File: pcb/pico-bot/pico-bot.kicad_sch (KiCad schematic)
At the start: 58 parts, among them J1 Conn_01x02_Male, J2 Conn_01x06_Male, J3 Conn_01x06_Male, J4 Conn_01x06_Male, J5 Conn_01x04_Male, Q1 DMG2305UX, Q2 AOD417, SW1 SW_SPDT, SW2 SW_Push, SW3 SW_Push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

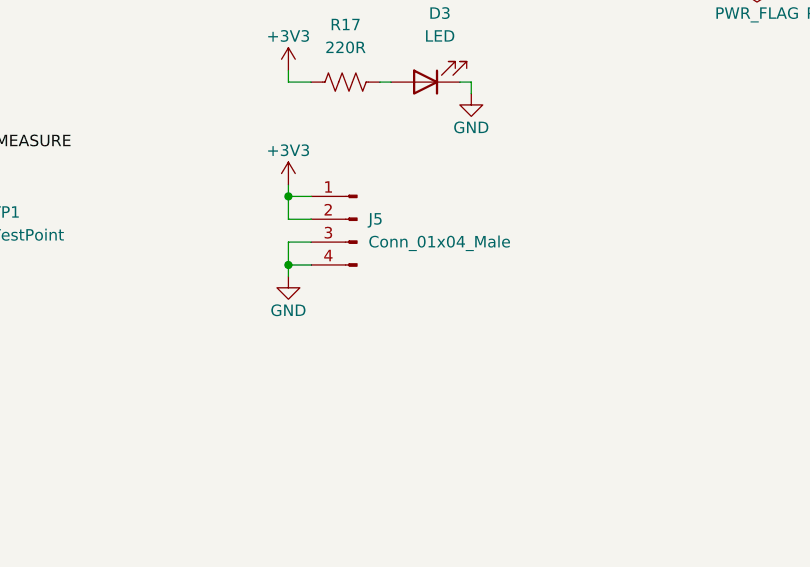
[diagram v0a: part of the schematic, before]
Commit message: Fix missing footprints, add parts to PCB
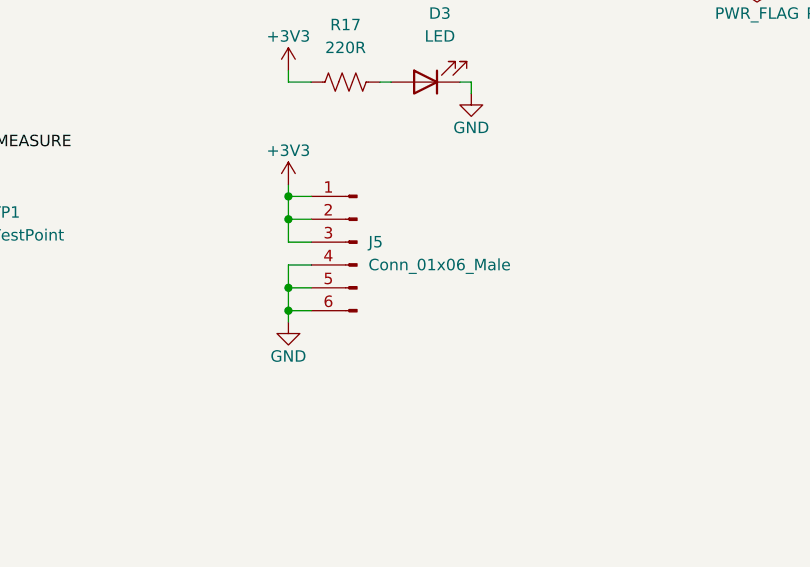
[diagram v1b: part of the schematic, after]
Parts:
- removed J5: Conn_01x04_Male, symbol Connector:Conn_01x04_Male
- added J5: Conn_01x06_Male, Connector_PinHeader_2.54mm:PinHeader_2x03_P2.54mm_Vertical, symbol Connector:Conn_01x06_Male
- J4: footprint Connector_PinHeader_2.54mm:PinHeader_1x06_P2.54mm_Vertical -> Connector_PinHeader_2.54mm:PinHeader_2x03_P2.54mm_Vertical
- SW1: footprint (none) -> pico-bot:1101M2S3CRE2
- U4: footprint RPi_Pico:RPi_Pico_SMD_TH -> pico-bot:RPi_Pico_SMD_TH
- U5: footprint (none) -> Package_SO:SOIC-8-1EP_3.9x4.9mm_P1.27mm_EP2.29x3mm
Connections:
- net +3V3: now also J5.1 (Pin_1), J5.2 (Pin_2), J5.3 (Pin_3)
- net GND: now also J5.4 (Pin_4), J5.5 (Pin_5), J5.6 (Pin_6)
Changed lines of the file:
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@@
   (junction (at 182.88 148.59) (diameter 0) (color 0 0 0 0)
   )
-  (junction (at 281.94 86.36) (diameter 0) (color 0 0 0 0)
+  (junction (at 281.94 91.44) (diameter 0) (color 0 0 0 0)
   )
   (junction (at 308.61 233.68) (diameter 0) (color 0 0 0 0)
@@
   (junction (at 171.45 39.37) (diameter 0) (color 0 0 0 0)
   )
+  (junction (at 281.94 81.28) (diameter 0) (color 0 0 0 0)
+  )
   (junction (at 181.61 39.37) (diameter 0) (color 0 0 0 0)
   )
@@
   (junction (at 171.45 50.8) (diameter 0) (color 0 0 0 0)
   )
+  (junction (at 281.94 88.9) (diameter 0) (color 0 0 0 0)
+  )
   (junction (at 281.94 78.74) (diameter 0) (color 0 0 0 0)
   )
@@
     (stroke (width 0) (type default) (color 0 0 0 0))
   )
-  (wire (pts (xy 281.94 86.36) (xy 281.94 87.63))
+  (wire (pts (xy 281.94 91.44) (xy 281.94 92.71))
     (stroke (width 0) (type default) (color 0 0 0 0))
   )
@@
     (stroke (width 0) (type default) (color 0 0 0 0))
   )
+  (wire (pts (xy 284.48 86.36) (xy 281.94 86.36))
+    (stroke (width 0) (type default) (color 0 0 0 0))
+  )
   (wire (pts (xy 217.17 185.42) (xy 217.17 184.15))
     (stroke (width 0) (type default) (color 0 0 0 0))
@@
     (stroke (width 0) (type default) (color 0 0 0 0))
   )
+  (wire (pts (xy 281.94 86.36) (xy 281.94 88.9))
+    (stroke (width 0) (type default) (color 0 0 0 0))
+  )
   (wire (pts (xy 247.65 205.74) (xy 248.92 205.74))
     (stroke (width 0) (type default) (color 0 0 0 0))
@@
     (stroke (width 0) (type default) (color 0 0 0 0))
   )
-  (wire (pts (xy 281.94 83.82) (xy 281.94 86.36))
+  (wire (pts (xy 281.94 88.9) (xy 281.94 91.44))
     (stroke (width 0) (type default) (color 0 0 0 0))
   )
@@
     (stroke (width 0) (type default) (color 0 0 0 0))
   )
-  (wire (pts (xy 281.94 86.36) (xy 284.48 86.36))
+  (wire (pts (xy 281.94 91.44) (xy 284.48 91.44))
     (stroke (width 0) (type default) (color 0 0 0 0))
   )
@@
     (stroke (width 0) (type default) (color 0 0 0 0))
   )
+  (wire (pts (xy 284.48 83.82) (xy 281.94 83.82))
+    (stroke (width 0) (type default) (color 0 0 0 0))
+  )
   (wire (pts (xy 307.34 228.6) (xy 308.61 228.6))
     (stroke (width 0) (type default) (color 0 0 0 0))
@@
     (stroke (width 0) (type default) (color 0 0 0 0))
   )
+  (wire (pts (xy 281.94 83.82) (xy 281.94 81.28))
+    (stroke (width 0) (type default) (color 0 0 0 0))
+  )
   (wire (pts (xy 259.08 205.74) (xy 260.35 205.74))
     (stroke (width 0) (type default) (color 0 0 0 0))
@@
     (stroke (width 0) (type default) (color 0 0 0 0))
   )
-  (wire (pts (xy 284.48 83.82) (xy 281.94 83.82))
+  (wire (pts (xy 284.48 88.9) (xy 281.94 88.9))
     (stroke (width 0) (type default) (color 0 0 0 0))
   )
@@
     (property "Reference" "SW1" (id 0) (at 148.59 34.29 0))
     (property "Value" "SW_SPDT" (id 1) (at 148.59 36.83 0))
-    (property "Footprint" "" (id 2) (at 148.59 41.91 0)
+    (property "Footprint" "pico-bot:1101M2S3CRE2" (id 2) (at 148.59 41.91 0)
       (effects (font (size 1.27 1.27)) hide)
     )
@@
     (property "Reference" "U5" (id 0) (at 231.14 63.5 0))
     (property "Value" "TL062" (id 1) (at 231.14 66.04 0))
-    (property "Footprint" "" (id 2) (at 231.14 73.66 0)
+    (property "Footprint" "Package_SO:SOIC-8-1EP_3.9x4.9mm_P1.27mm_EP2.29x3mm" (id 2) (at 231.14 73.66 0)
       (effects (font (size 1.27 1.27)) hide)
     )
@@
     (pin "2")
   )
-  (symbol (lib_id "Connector:Conn_01x04_Male") (at 289.56 81.28 0) (mirror y) (unit 1)
-    (in_bom yes) (on_board yes) (fields_autoplaced)
-    (property "Reference" "J5" (id 0) (at 290.83 81.2799 0)
-      (effects (font (size 1.27 1.27)) (justify right))
-    )
-    (property "Value" "Conn_01x04_Male" (id 1) (at 290.83 83.8199 0)
-      (effects (font (size 1.27 1.27)) (justify right))
-    )
-    (property "Footprint" "" (id 2) (at 289.56 81.28 0)
-      (effects (font (size 1.27 1.27)) hide)
-    )
-    (property "Datasheet" "~" (id 3) (at 289.56 81.28 0)
-      (effects (font (size 1.27 1.27)) hide)
-    )
-    (pin "1")
-    (pin "2")
-    (pin "3")
-    (pin "4")
-  )
   (symbol (lib_id "Device:C") (at 297.18 185.42 180) (unit 1)
     (in_bom yes) (on_board yes) (fields_autoplaced)
@@
     (pin "2")
   )
+  (symbol (lib_id "Connector:Conn_01x06_Male") (at 289.56 83.82 0) (mirror y) (unit 1)
+    (in_bom yes) (on_board yes) (fields_autoplaced)
+    (property "Reference" "J5" (id 0) (at 290.83 83.8199 0)
+      (effects (font (size 1.27 1.27)) (justify right))
+    )
+    (property "Value" "Conn_01x06_Male" (id 1) (at 290.83 86.3599 0)
+      (effects (font (size 1.27 1.27)) (justify right))
+    )
+    (property "Footprint" "Connector_PinHeader_2.54mm:PinHeader_2x03_P2.54mm_Vertical" (id 2) (at 289.56 83.82 0)
+      (effects (font (size 1.27 1.27)) hide)
+    )
+    (property "Datasheet" "~" (id 3) (at 289.56 83.82 0)
+      (effects (font (size 1.27 1.27)) hide)
+    )
+    (pin "1")
+    (pin "2")
+    (pin "3")
+    (pin "4")
+    (pin "5")
+    (pin "6")
+  )
   (symbol (lib_id "Device:C") (at 269.24 185.42 180) (unit 1)
     (in_bom yes) (on_board yes) (fields_autoplaced)
@@
       (effects (font (size 1.27 1.27)) (justify left))
     )
-    (property "Footprint" "" (id 2) (at 233.68 95.25 0)
+    (property "Footprint" "Package_SO:SOIC-8-1EP_3.9x4.9mm_P1.27mm_EP2.29x3mm" (id 2) (at 233.68 95.25 0)
       (effects (font (size 1.27 1.27)) hide)
     )
@@
     (property "Reference" "U4" (id 0) (at 198.12 177.8 0))
     (property "Value" "Pico W" (id 1) (at 198.12 180.34 0))
-    (property "Footprint" "RPi_Pico:RPi_Pico_SMD_TH" (id 2) (at 198.12 209.55 90)
+    (property "Footprint" "pico-bot:RPi_Pico_SMD_TH" (id 2) (at 198.12 209.55 90)
       (effects (font (size 1.27 1.27)) hide)
     )
@@
     (pin "1")
   )
-  (symbol (lib_id "power:GND") (at 281.94 87.63 0) (unit 1)
+  (symbol (lib_id "power:GND") (at 281.94 92.71 0) (unit 1)
     (in_bom yes) (on_board yes)
-    (property "Reference" "#PWR084" (id 0) (at 281.94 93.98 0)
+    (property "Reference" "#PWR084" (id 0) (at 281.94 99.06 0)
       (effects (font (size 1.27 1.27)) hide)
     )
-    (property "Value" "GND" (id 1) (at 281.94 91.44 0))
-    (property "Footprint" "" (id 2) (at 281.94 87.63 0)
+    (property "Value" "GND" (id 1) (at 281.94 96.52 0))
+    (property "Footprint" "" (id 2) (at 281.94 92.71 0)
       (effects (font (size 1.27 1.27)) hide)
     )
-    (property "Datasheet" "" (id 3) (at 281.94 87.63 0)
+    (property "Datasheet" "" (id 3) (at 281.94 92.71 0)
       (effects (font (size 1.27 1.27)) hide)
     )
@@
       (effects (font (size 1.27 1.27)) (justify right))
     )
-    (property "Footprint" "Connector_PinHeader_2.54mm:PinHeader_1x06_P2.54mm_Vertical" (id 2) (at 205.74 246.38 0)
+    (property "Footprint" "Connector_PinHeader_2.54mm:PinHeader_2x03_P2.54mm_Vertical" (id 2) (at 205.74 246.38 0)
       (effects (font (size 1.27 1.27)) hide)
     )
@@
     )
     (path "/f3d5a8ae-9458-4fad-b625-d11ebc72ab12"
-      (reference "J4") (unit 1) (value "Conn_01x06_Male") (footprint "Connector_PinHeader_2.54mm:PinHeader_1x06_P2.54mm_Vertical")
+      (reference "J4") (unit 1) (value "Conn_01x06_Male") (footprint "Connector_PinHeader_2.54mm:PinHeader_2x03_P2.54mm_Vertical")
     )
-    (path "/2de5aca8-3021-4cd1-86bb-3bf196f88b8c"
-      (reference "J5") (unit 1) (value "Conn_01x04_Male") (footprint "")
+    (path "/54826259-a4b8-4af5-b44d-c554d746d903"
+      (reference "J5") (unit 1) (value "Conn_01x06_Male") (footprint "Connector_PinHeader_2.54mm:PinHeader_2x03_P2.54mm_Vertical")
     )
     (path "/6cbd6e90-66d2-4528-9d84-e3c48ceb7a1b"
@@
     )
     (path "/0b3e63f7-acf6-4f89-bb34-87de3fe9651b"
-      (reference "SW1") (unit 1) (value "SW_SPDT") (footprint "")
+      (reference "SW1") (unit 1) (value "SW_SPDT") (footprint "pico-bot:1101M2S3CRE2")
     )
     (path "/69164c6f-c053-48be-b784-910902d2eae0"
@@
     )
     (path "/ad07bf90-bfab-42b0-b28c-888c2b38f1e3"
-      (reference "U4") (unit 1) (value "Pico W") (footprint "RPi_Pico:RPi_Pico_SMD_TH")
+      (reference "U4") (unit 1) (value "Pico W") (footprint "pico-bot:RPi_Pico_SMD_TH")
     )
     (path "/c5a8208e-a214-48c6-bde6-d62db21833ce"
@@
     )
     (path "/0e4f0a6f-a2ec-472e-a871-ba2595a81c5f"
-      (reference "U5") (unit 2) (value "TL062") (footprint "")
+      (reference "U5") (unit 2) (value "TL062") (footprint "Package_SO:SOIC-8-1EP_3.9x4.9mm_P1.27mm_EP2.29x3mm")
     )
     (path "/6ec2ccf4-79f6-434e-8812-072b71eb377e"
-      (reference "U5") (unit 3) (value "TL062") (footprint "")
+      (reference "U5") (unit 3) (value "TL062") (footprint "Package_SO:SOIC-8-1EP_3.9x4.9mm_P1.27mm_EP2.29x3mm")
     )
     (path "/625748c1-ad21-482b-8283-5149d5773445"

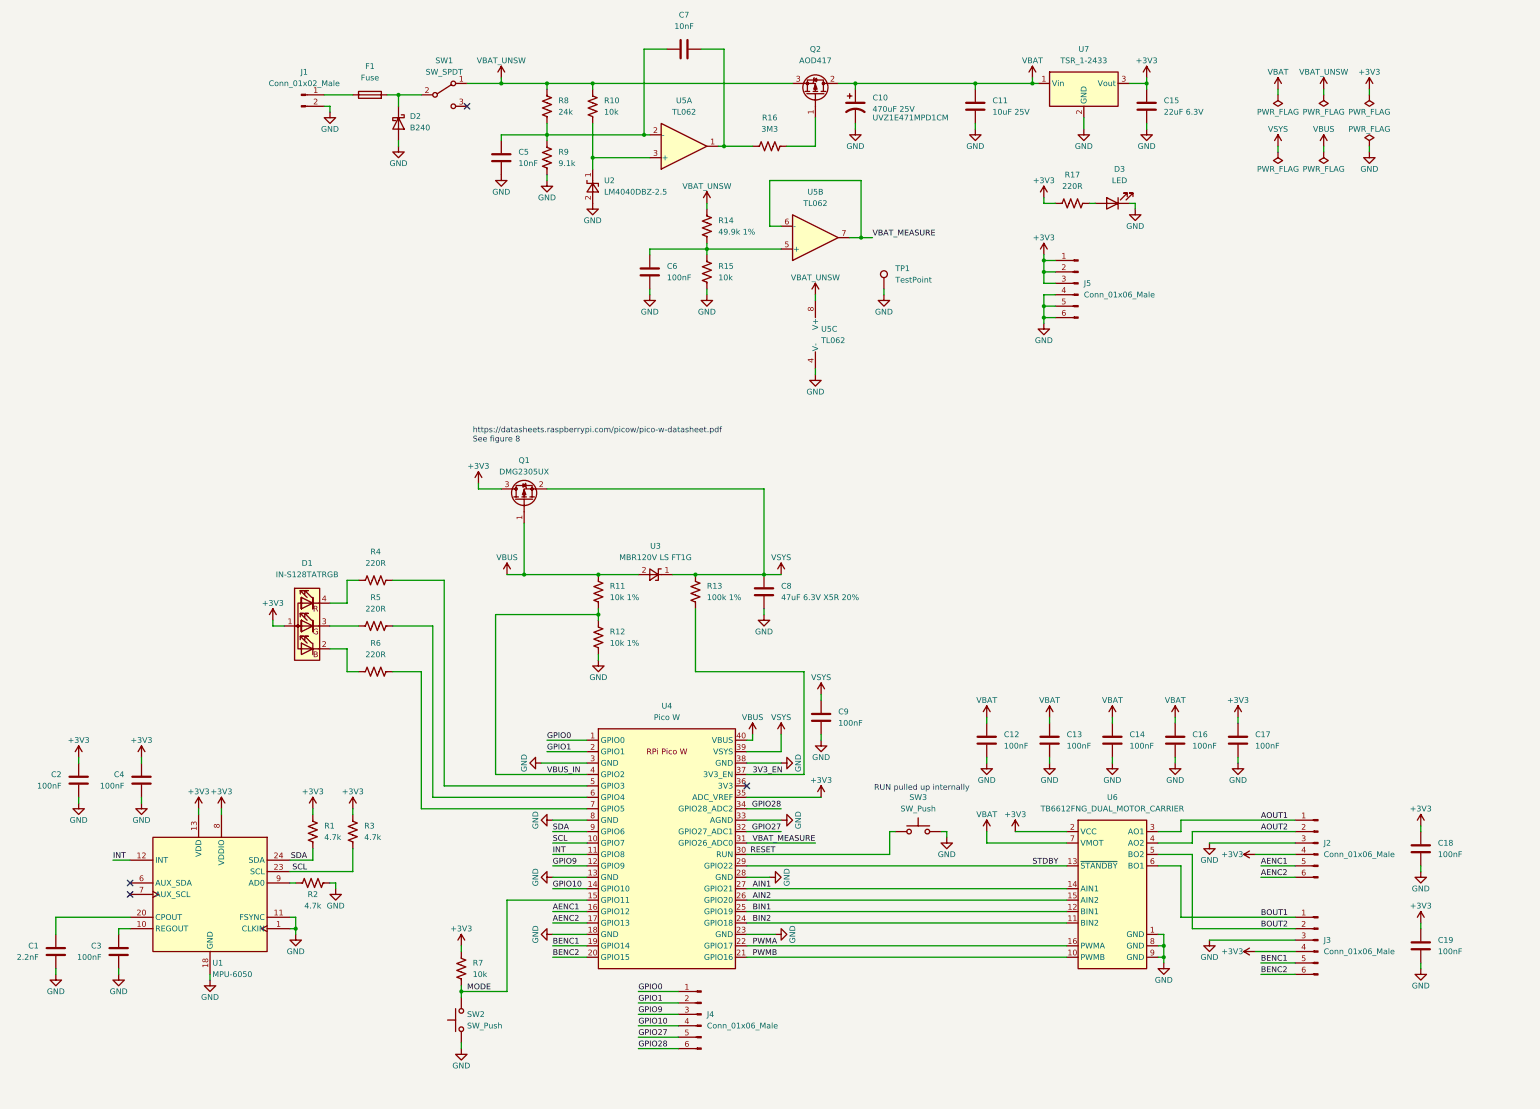
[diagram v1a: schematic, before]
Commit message: Rework pin allocation to ease layout
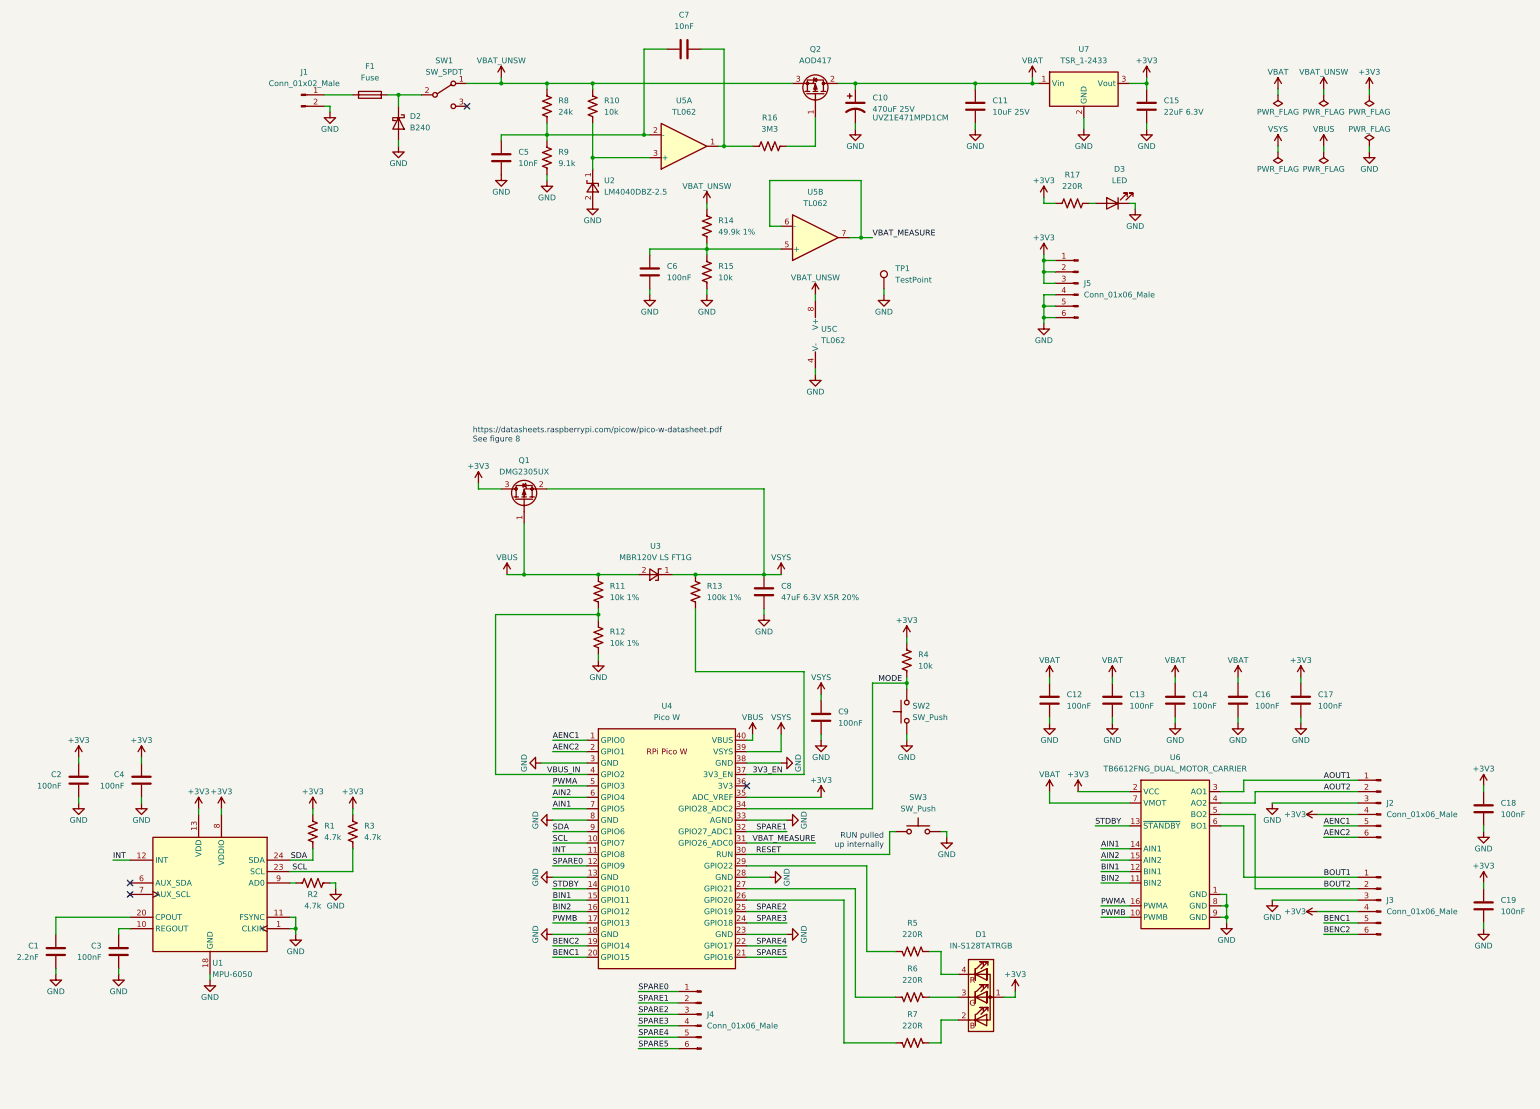
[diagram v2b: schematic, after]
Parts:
- R4: value 220R -> 10k
- R7: value 10k -> 220R
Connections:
- net +3V3: now also R4.2; no longer R7.2
- net AENC1: now also U4.1 (GPIO0); no longer U4.16 (GPIO12)
- net AENC2: now also U4.2 (GPIO1); no longer U4.17 (GPIO13)
- net AIN1: now also U4.7 (GPIO5); no longer U4.27 (GPIO21)
- net AIN2: now also U4.6 (GPIO4); no longer U4.26 (GPIO20)
- net BENC1: now also U4.20 (GPIO15); no longer U4.19 (GPIO14)
- net BENC2: now also U4.19 (GPIO14); no longer U4.20 (GPIO15)
- net BIN1: now also U4.15 (GPIO11); no longer U4.25 (GPIO19)
- net BIN2: now also U4.16 (GPIO12); no longer U4.24 (GPIO18)
- net MODE: now also R4.1, U4.34 (GPIO28_ADC2); no longer R7.1, U4.15 (GPIO11)
- net PWMA: now also U4.5 (GPIO3); no longer U4.22 (GPIO17)
- net PWMB: now also U4.17 (GPIO13); no longer U4.21 (GPIO16)
- net STDBY: now also U4.14 (GPIO10); no longer U4.29 (GPIO22)
- net at D1.2 (BK): now also R7.1; no longer R6.1
- net at R5.1: now also D1.4 (RK); no longer D1.3 (GK)
- net at R5.2: now also U4.29 (GPIO22); no longer U4.6 (GPIO4)
- net at R6.2: now also U4.27 (GPIO21); no longer U4.7 (GPIO5)
- net GPIO0 renamed SPARE0
- net SPARE0: now also U4.12 (GPIO9); no longer U4.1 (GPIO0)
- net GPIO1 renamed SPARE1
- net SPARE1: now also U4.32 (GPIO27_ADC1); no longer U4.2 (GPIO1)
- net GPIO10 renamed SPARE3
- net SPARE3: now also U4.24 (GPIO18); no longer U4.14 (GPIO10)
- net GPIO27 renamed SPARE4
- net SPARE4: now also U4.22 (GPIO17); no longer U4.32 (GPIO27_ADC1)
- net GPIO28 renamed SPARE5
- net SPARE5: now also U4.21 (GPIO16); no longer U4.34 (GPIO28_ADC2)
- net GPIO9 renamed SPARE2
- net SPARE2: now also U4.25 (GPIO19); no longer U4.12 (GPIO9)
- new net: D1.3 (GK), R6.1
- new net: R7.2, U4.26 (GPIO20)
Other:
- moved on the sheet: C12, C13, C14, C16, C17, C18, C19, J2, J3, U6

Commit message: Route all except power and ground
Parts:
- removed J4, J5: Conn_01x06_Male, Connector_PinHeader_2.54mm:PinHeader_2x03_P2.54mm_Vertical, symbol Connector:Conn_01x06_Male
- added J4: Conn_01x08_Male, Connector_PinHeader_2.54mm:PinHeader_2x04_P2.54mm_Vertical, symbol Connector:Conn_01x08_Male
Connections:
- net SPARE4 is gone; now on net SPARE2: U4.22 (GPIO17)
- net SPARE5 is gone; now on net SPARE3: U4.21 (GPIO16)
- net +3V3: now also J4.2 (Pin_2), J4.4 (Pin_4)
- net GND: now also J4.6 (Pin_6), J4.8 (Pin_8)
- net SPARE0: now also U4.25 (GPIO19), J4.1 (Pin_1); no longer U4.12 (GPIO9)
- net SPARE1: now also U4.24 (GPIO18), J4.3 (Pin_3); no longer U4.32 (GPIO27_ADC1)
- net SPARE2: now also J4.5 (Pin_5); no longer U4.25 (GPIO19)
- net SPARE3: now also J4.7 (Pin_7); no longer U4.24 (GPIO18)
- net at R7.2: now also U4.27 (GPIO21); no longer U4.26 (GPIO20)
- net at R6.2: now also U4.26 (GPIO20); no longer U4.27 (GPIO21)
- no-connect marks 4 -> 6
